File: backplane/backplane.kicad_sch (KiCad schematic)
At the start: 5 parts, among them J1 Interface Driver, J2 Interface Additional, J3 USB_B, J5 Interface Core

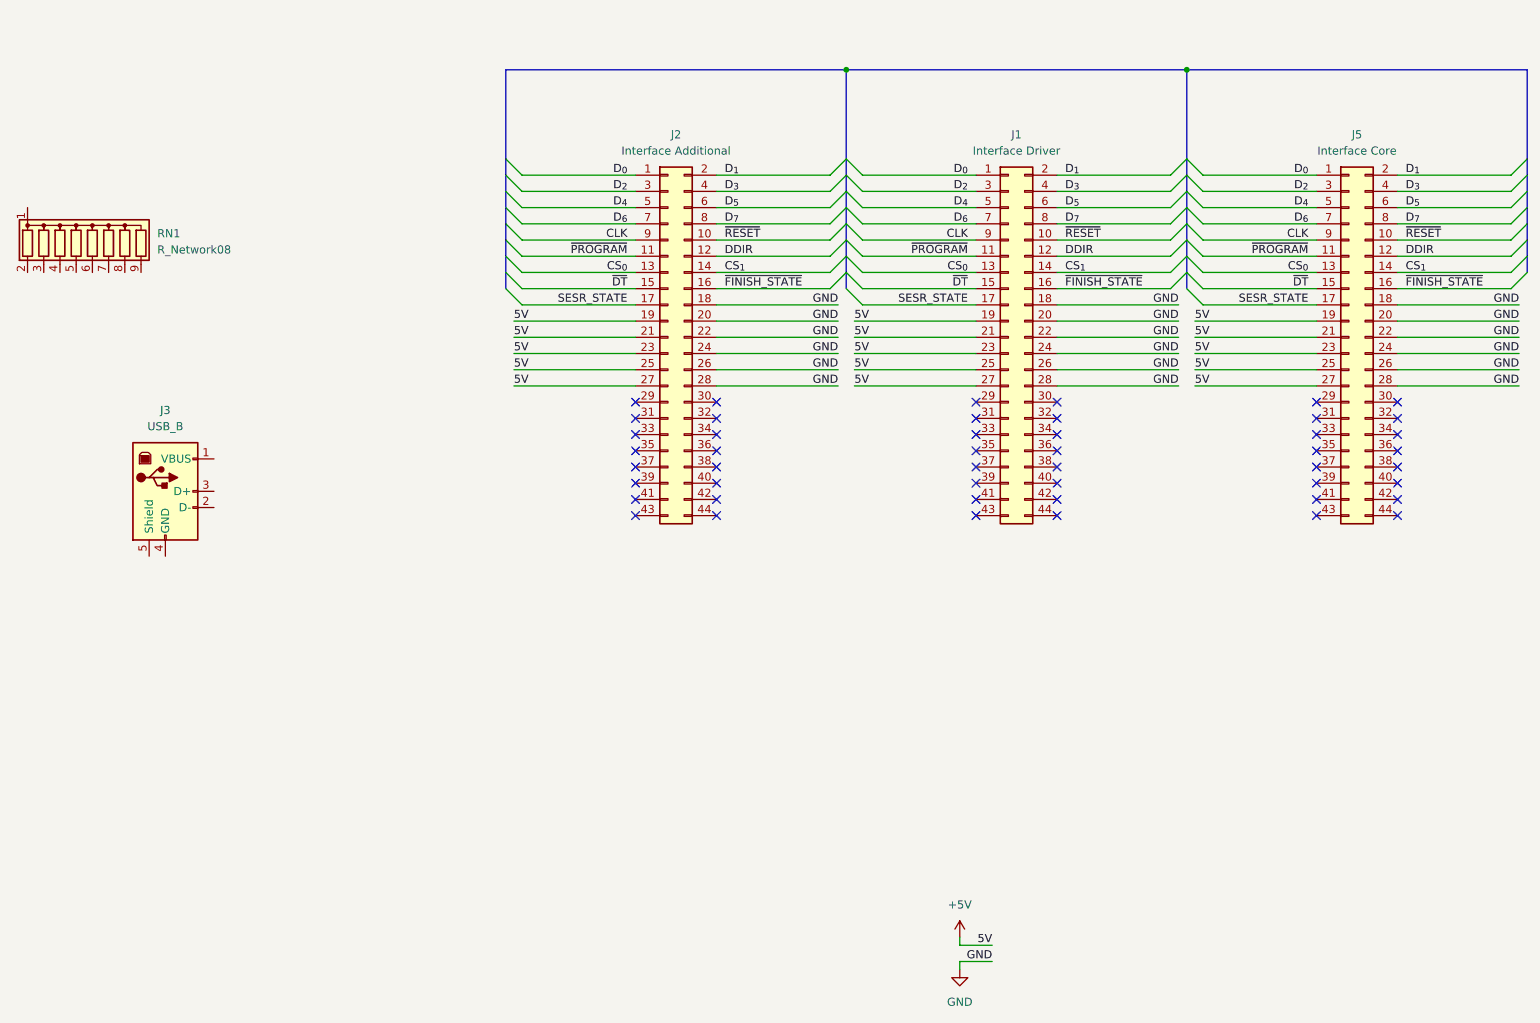
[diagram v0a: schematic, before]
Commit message: added backplane PCB and adjusted driver silkscreen text thickness
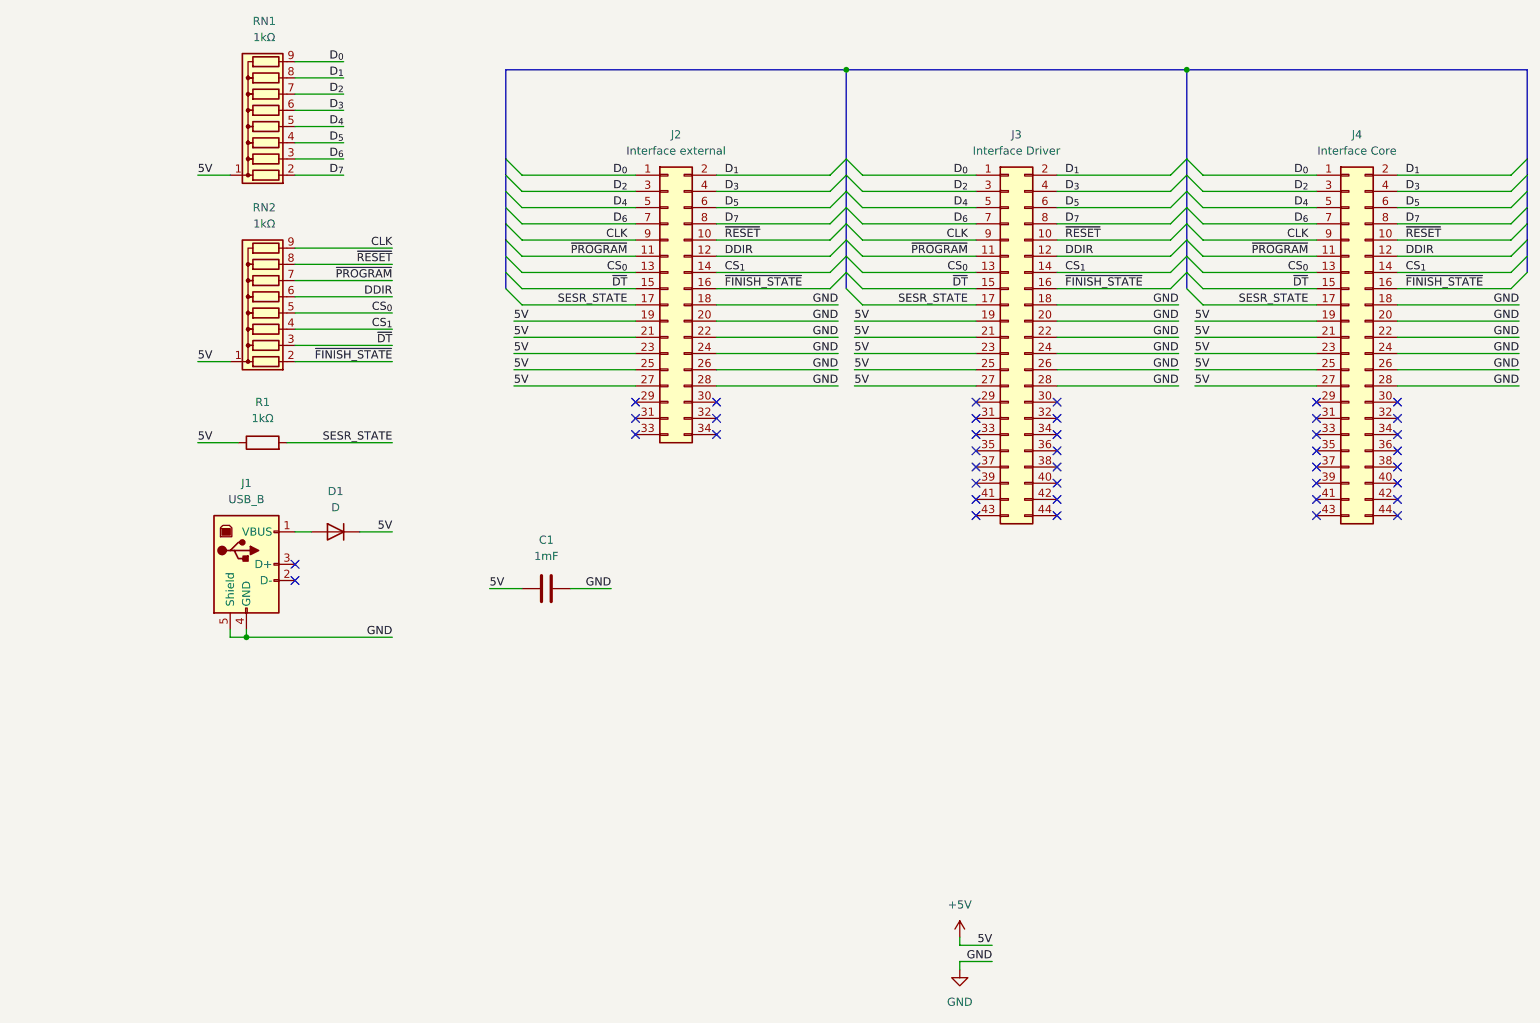
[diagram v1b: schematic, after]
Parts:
- removed J2: Interface Additional, Connector_IDC:IDC-Header_2x22_P2.54mm_Vertical, symbol Connector_Generic:Conn_02x22_Odd_Even
- added C1: 1mF, Capacitor_THT:C_Radial_D12.5mm_H20.0mm_P5.00mm, symbol Device:C
- added D1: D, Diode_THT:D_DO-35_SOD27_P10.16mm_Horizontal, symbol Device:D
- added J2: Interface external, Connector_IDC:IDC-Header_2x17_P2.54mm_Vertical, symbol Connector_Generic:Conn_02x17_Odd_Even
- added R1: 1kΩ, symbol Device:R
- added RN2: 1kΩ, Resistor_THT:R_Array_SIP9, symbol Device:R_Network08
- J1: renamed from J3; footprint (none) -> Connector_USB:USB_B_OST_USB-B1HSxx_Horizontal
- RN1: value R_Network08 -> 1kΩ
- renumbered J1 to J3, J5 to J4
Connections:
- net +5V: now also RN1.1 (common), C1.1, D1.1 (K), J2.19 (Pin_19), J2.21 (Pin_21), J2.23 (Pin_23), J2.25 (Pin_25), J2.27 (Pin_27), R1.1, RN2.1 (common)
- net CLK: now also J2.9 (Pin_9), RN2.9 (R8)
- net CS_{0}: now also J2.13 (Pin_13), RN2.5 (R4)
- net CS_{1}: now also J2.14 (Pin_14), RN2.4 (R3)
- net DDIR: now also J2.12 (Pin_12), RN2.6 (R5)
- net D_{0}: now also RN1.9 (R8), J2.1 (Pin_1)
- net D_{1}: now also RN1.8 (R7), J2.2 (Pin_2)
- net D_{2}: now also RN1.7 (R6), J2.3 (Pin_3)
- net D_{3}: now also RN1.6 (R5), J2.4 (Pin_4)
- net D_{4}: now also RN1.5 (R4), J2.5 (Pin_5)
- net D_{5}: now also RN1.4 (R3), J2.6 (Pin_6)
- net D_{6}: now also RN1.3 (R2), J2.7 (Pin_7)
- net D_{7}: now also RN1.2 (R1), J2.8 (Pin_8)
- net GND: now also J1.4 (GND), J1.5 (Shield), C1.2, J2.18 (Pin_18), J2.20 (Pin_20), J2.22 (Pin_22), J2.24 (Pin_24), J2.26 (Pin_26), J2.28 (Pin_28)
- net SESR_STATE: now also J2.17 (Pin_17), R1.2
- net ~{DT}: now also J2.15 (Pin_15), RN2.3 (R2)
- net ~{FINISH_STATE}: now also J2.16 (Pin_16), RN2.2 (R1)
- net ~{PROGRAM}: now also J2.11 (Pin_11), RN2.7 (R6)
- net ~{RESET}: now also J2.10 (Pin_10), RN2.8 (R7)
- net at J1.1 (VBUS): now also D1.2 (A)
- no-connect marks 48 -> 40
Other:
- moved on the sheet: J1, RN1
